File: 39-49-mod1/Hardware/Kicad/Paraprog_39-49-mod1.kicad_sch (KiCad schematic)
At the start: 10 parts, among them J1 USB_A, U1 STM32F030C8Tx, U2 AMS1117-3.3

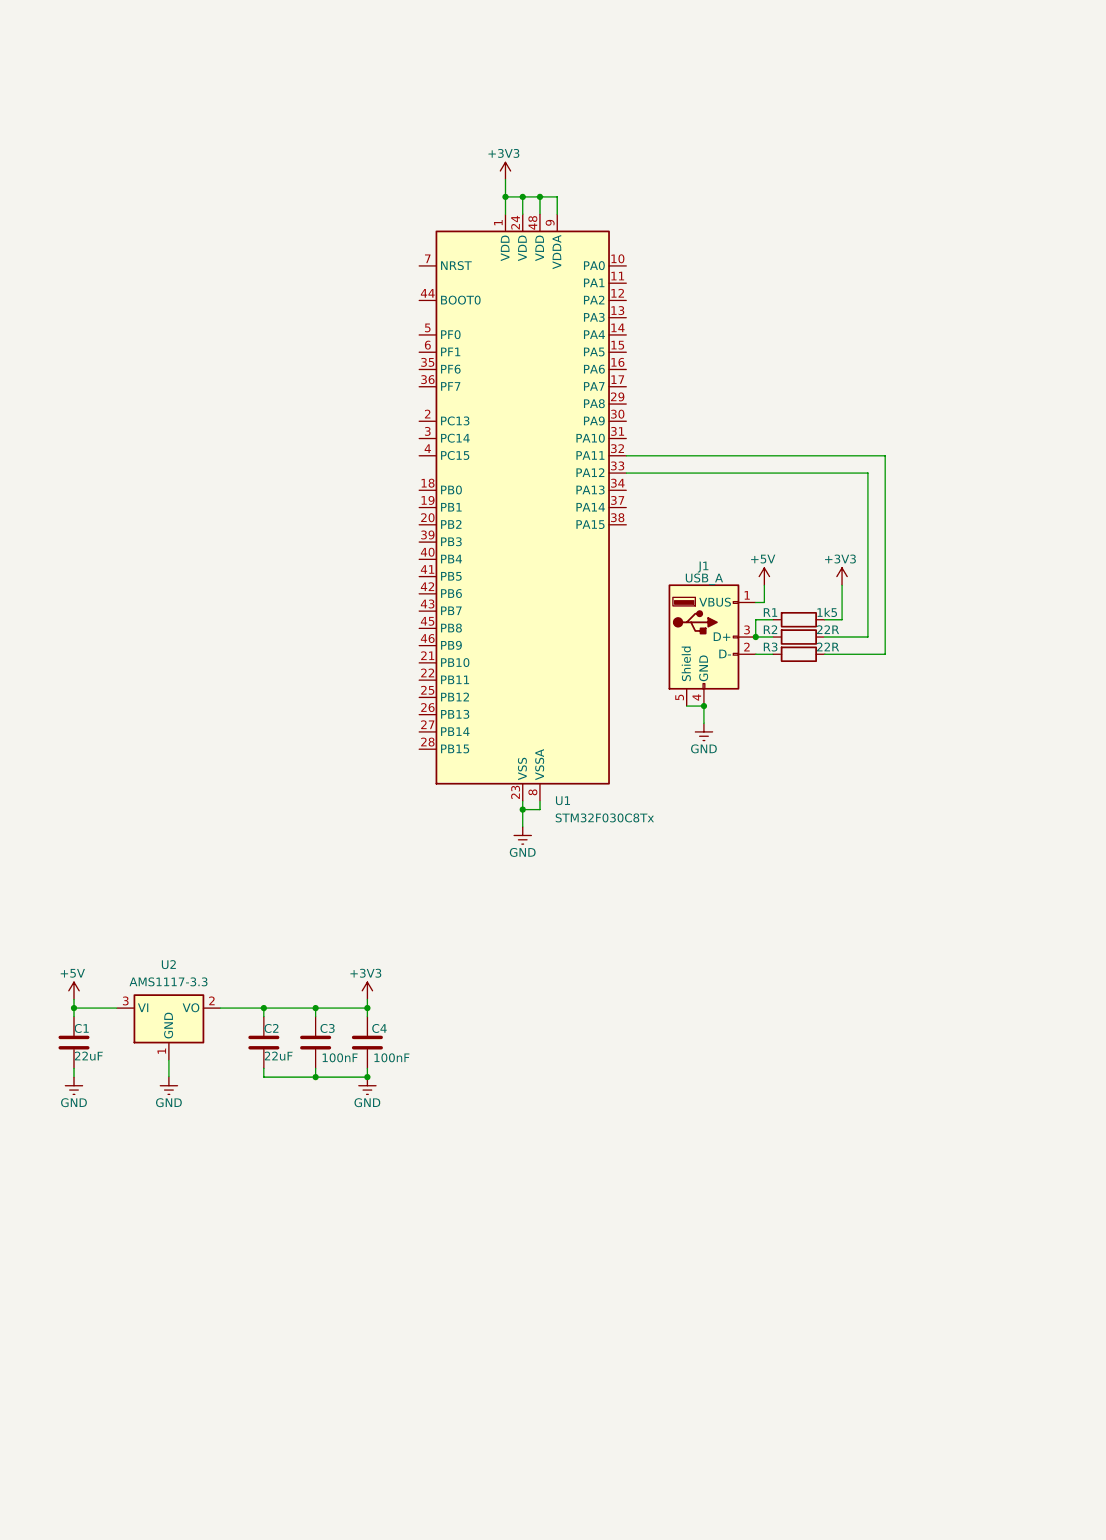
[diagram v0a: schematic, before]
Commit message: schematics for 39-49-mod1
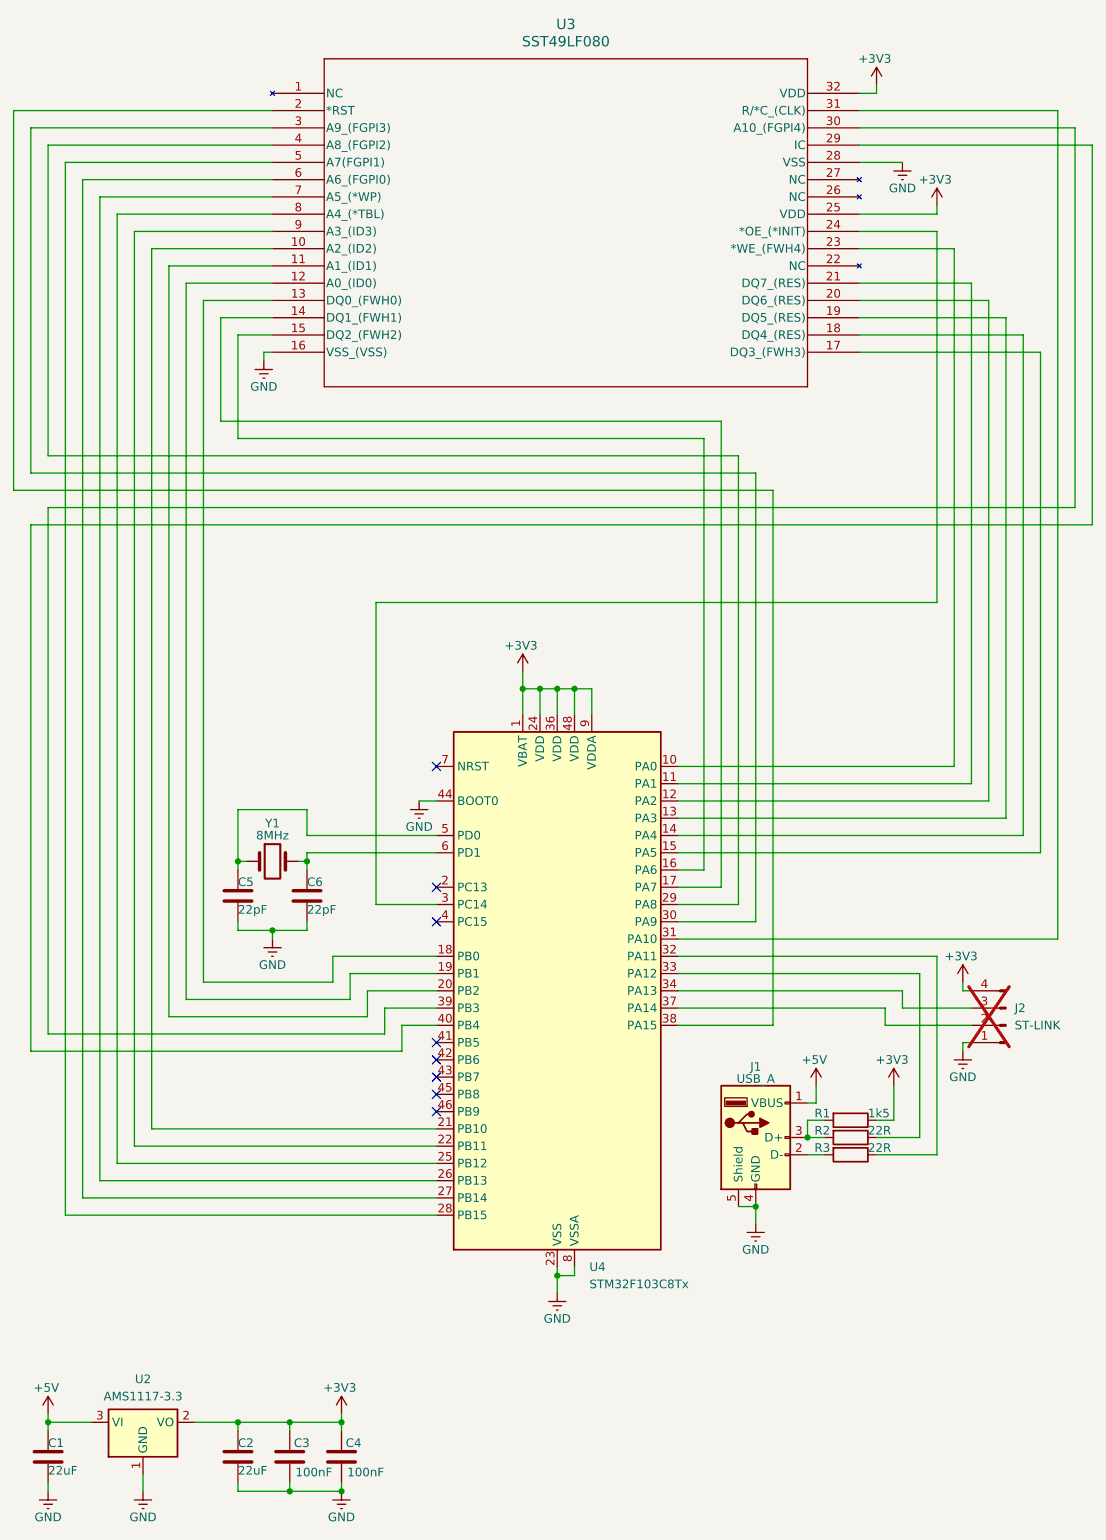
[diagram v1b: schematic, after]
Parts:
- removed U1: STM32F030C8Tx, Package_QFP:LQFP-48_7x7mm_P0.5mm, symbol MCU_ST_STM32F0:STM32F030C8Tx
- added C5, C6: 22pF, Capacitor_SMD:C_0805_2012Metric, symbol Device:C
- added J2: ST-LINK, Connector_PinHeader_2.54mm:PinHeader_1x04_P2.54mm_Vertical, symbol Connector:Conn_01x04_Pin
- added U3: SST49LF080, PLCC32_NH_SST_MCH, symbol 39-49-mod1:SST49LF080
- added U4: STM32F103C8Tx, Package_QFP:LQFP-48_7x7mm_P0.5mm, symbol MCU_ST_STM32F1:STM32F103C8Tx
- added Y1: 8MHz, Crystal:Crystal_HC49-U_Vertical, symbol Device:Crystal
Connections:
- net +3V3: now also J2.4 (Pin_4), U3.25 (VDD), U3.32 (VDD), U4.1 (VBAT), U4.24 (VDD), U4.36 (VDD), U4.48 (VDD), U4.9 (VDDA)
- net GND: now also C5.2, C6.2, J2.1 (Pin_1), U3.16 (VSS_(VSS)), U3.28 (VSS), U4.23 (VSS), U4.35 (VSS), U4.44 (BOOT0), U4.47 (VSS), U4.8 (VSSA)
- net at R3.1: now also U4.32 (PA11)
- net at R2.1: now also U4.33 (PA12)
- new net: C6.1, U4.6 (PD1), Y1.2
- new net: U3.23 (*WE_(FWH4)), U4.10 (PA0)
- new net: U3.21 (DQ7_(RES)), U4.11 (PA1)
- new net: U3.20 (DQ6_(RES)), U4.12 (PA2)
- new net: U3.19 (DQ5_(RES)), U4.13 (PA3)
- new net: U3.18 (DQ4_(RES)), U4.14 (PA4)
- new net: U3.17 (DQ3_(FWH3)), U4.15 (PA5)
- new net: U3.15 (DQ2_(FWH2)), U4.16 (PA6)
- new net: U3.14 (DQ1_(FWH1)), U4.17 (PA7)
- new net: U3.13 (DQ0_(FWH0)), U4.18 (PB0)
- new net: U3.12 (A0_(ID0)), U4.19 (PB1)
- new net: U3.11 (A1_(ID1)), U4.20 (PB2)
- new net: U3.10 (A2_(ID2)), U4.21 (PB10)
- new net: U3.9 (A3_(ID3)), U4.22 (PB11)
- new net: U3.8 (A4_(*TBL)), U4.25 (PB12)
- new net: U3.7 (A5_(*WP)), U4.26 (PB13)
- new net: U3.6 (A6_(FGPI0)), U4.27 (PB14)
- new net: U3.5 (A7(FGPI1)), U4.28 (PB15)
- new net: U3.4 (A8_(FGPI2)), U4.29 (PA8)
- new net: U3.24 (*OE_(*INIT)), U4.3 (PC14)
- new net: U3.3 (A9_(FGPI3)), U4.30 (PA9)
- new net: U3.31 (R/*C_(CLK)), U4.31 (PA10)
- new net: J2.3 (Pin_3), U4.34 (PA13)
- new net: J2.2 (Pin_2), U4.37 (PA14)
- new net: U3.2 (*RST), U4.38 (PA15)
- new net: U3.30 (A10_(FGPI4)), U4.39 (PB3)
- new net: U3.29 (IC), U4.40 (PB4)
- new net: C5.1, U4.5 (PD0), Y1.1
- no-connect marks 0 -> 8
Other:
- moved on the sheet: C1, C2, C3, C4, J1, R1, R2, R3, U2
